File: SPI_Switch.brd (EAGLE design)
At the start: 71 x 62.2 mm, 40 parts, among them J1 8516-4500PL, J2 1-406525-1, J3 1-406525-1, J4 0705510037, J5 0705510037, U1 TLE7230G, U2 SN74ABT126

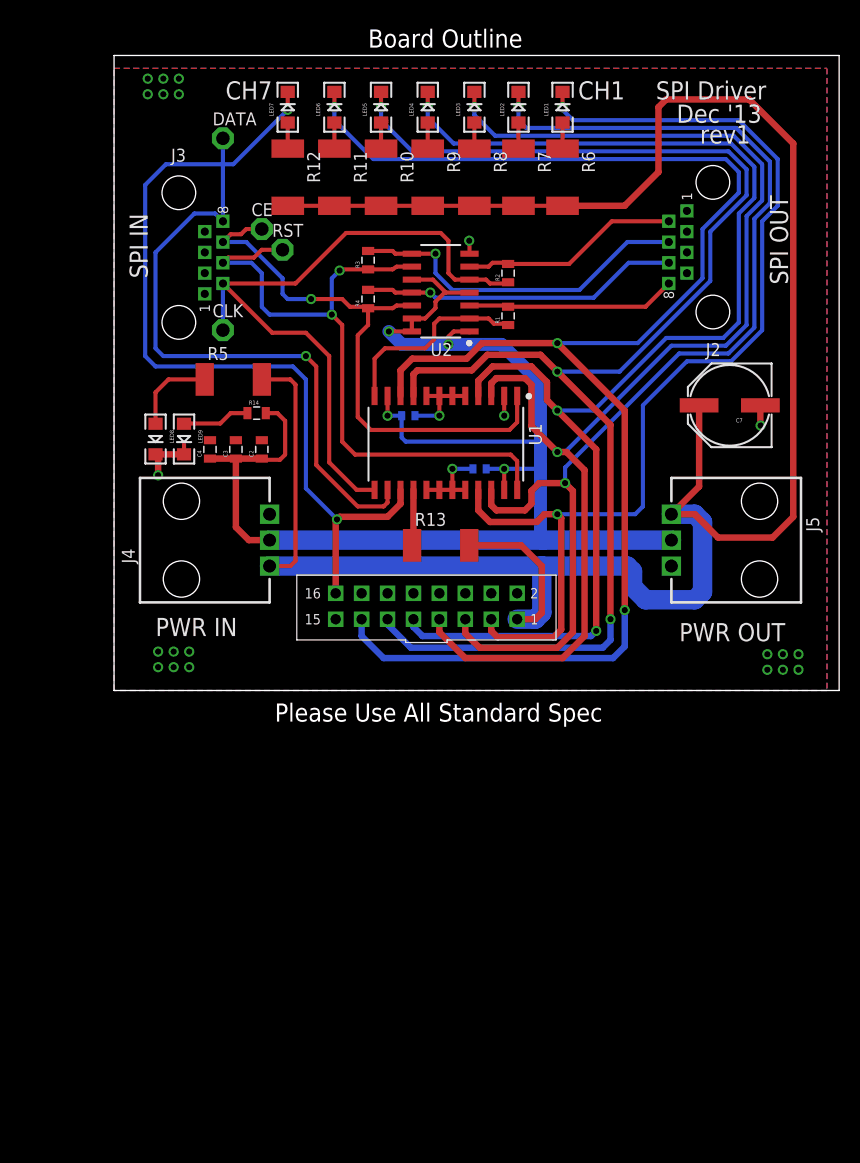
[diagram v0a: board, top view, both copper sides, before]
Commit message: Replaced decoupling caps for line driver with a larger package. Added smaller resistors for LEDs. Must ensure we never pull over 20mA with this resistor package.
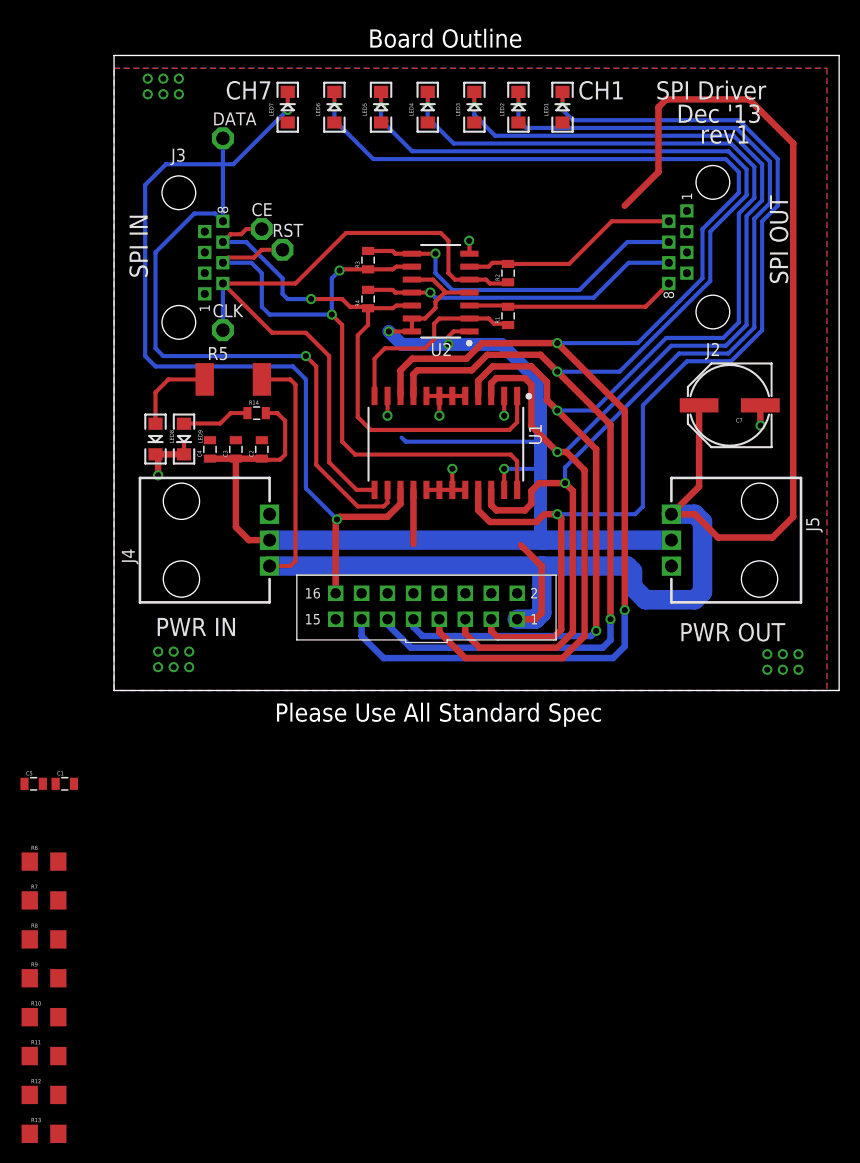
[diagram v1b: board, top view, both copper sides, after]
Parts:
- C1, C5: value (none) -> 10uF; device SparkFun-Passives:0402-CAP -> SparkFun-Passives:0805
- R10, R11, R12, R13, R6, R7, R8, R9: value 2k -> 1.5k; device SparkFun-Passives:R2512 -> SparkFun-Passives:1206
- moved R12 93.0 mm to (-6.86, -39.6), turned to 0 degrees
- moved R11 90.7 mm to (-6.86, -35.8), turned to 0 degrees
- moved R10 88.7 mm to (-6.86, -32.0), turned to 0 degrees
- moved R9 87.0 mm to (-6.86, -28.2), turned to 0 degrees
- moved R8 85.8 mm to (-6.86, -24.4), turned to 0 degrees
- moved R7 84.8 mm to (-6.86, -20.6), turned to 0 degrees
- moved R6 84.1 mm to (-6.86, -16.8), turned to 0 degrees
- moved R13 69.5 mm to (-6.86, -43.4)
- moved C5 53.5 mm to (-7.87, -9.14), flipped to the top
- moved C1 49.3 mm to (-4.83, -9.14), flipped to the top, turned to 0 degrees
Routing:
- net +24V: track 222.6 -> 184.5 mm
- net +5V: track 140.0 -> 134.7 mm
- net GND: track 27.3 -> 22.9 mm
- net N$7: track 4.03 -> 1.25 mm
- net N$9: track 2.56 -> 0.00 mm
- net N$8: track 2.56 -> 0.00 mm
- net N$6: track 2.56 -> 0.00 mm
- net N$5: track 2.56 -> 0.00 mm
- net N$3: track 2.56 -> 0.00 mm
- net N$1: track 2.56 -> 0.00 mm

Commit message: redoing layout
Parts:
- added H1, H2, H3, H4: MOUNT-HOLE2.8, holes:2,8
- moved J1 6.11 mm to (43.8, 2.67)
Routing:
- net CH6: track 153.5 -> 73.2 mm, vias 3 -> 2
- net CH5: track 141.4 -> 71.6 mm, vias 3 -> 2
- net CH4: track 128.8 -> 73.7 mm, vias 3 -> 2
- net CH3: track 123.2 -> 72.8 mm
- net +24V: track 184.5 -> 136.0 mm
- net CH2: track 110.6 -> 71.7 mm
- net CH1: track 106.1 -> 75.6 mm
- net CH7: track 82.7 -> 67.2 mm
- net CH8: track 5.30 -> 0.00 mm
- net GND: vias 23 -> 5

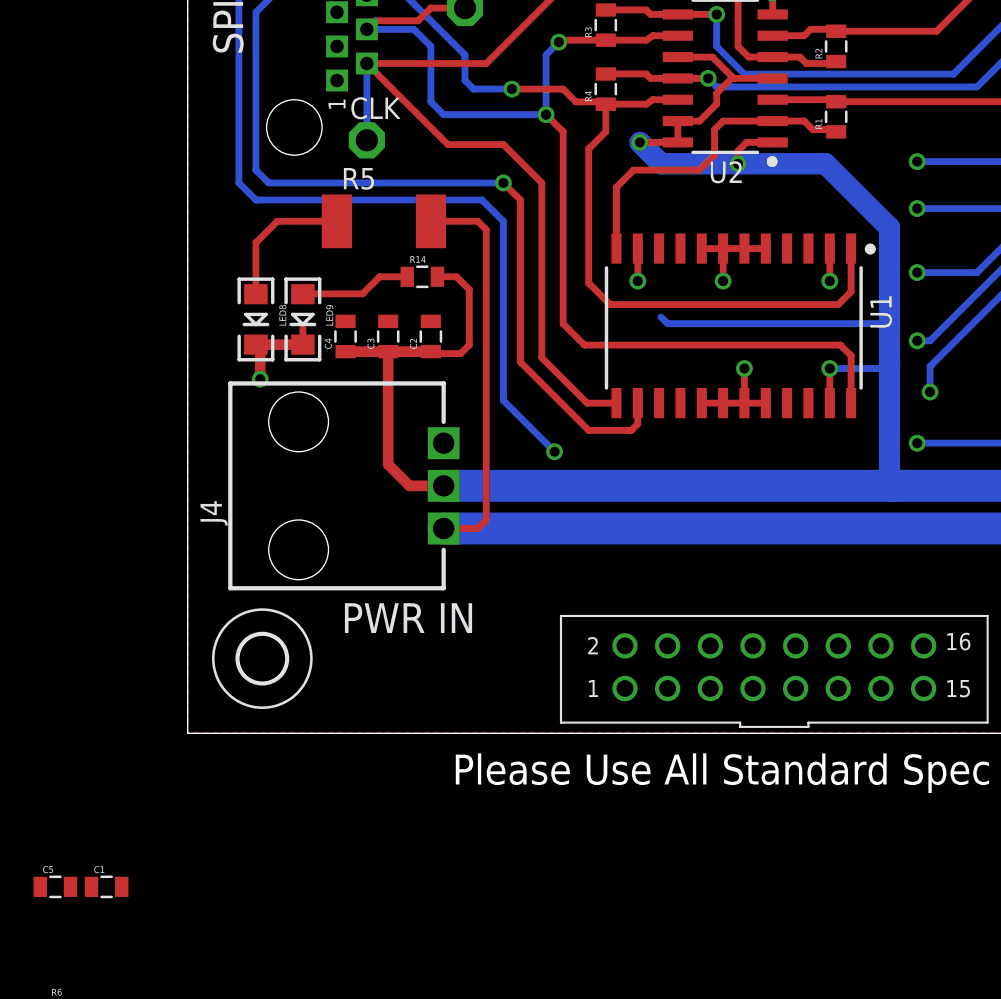
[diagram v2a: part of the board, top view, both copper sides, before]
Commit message: Redid layout again get rid of data out crossing 5V. Time to re-route.
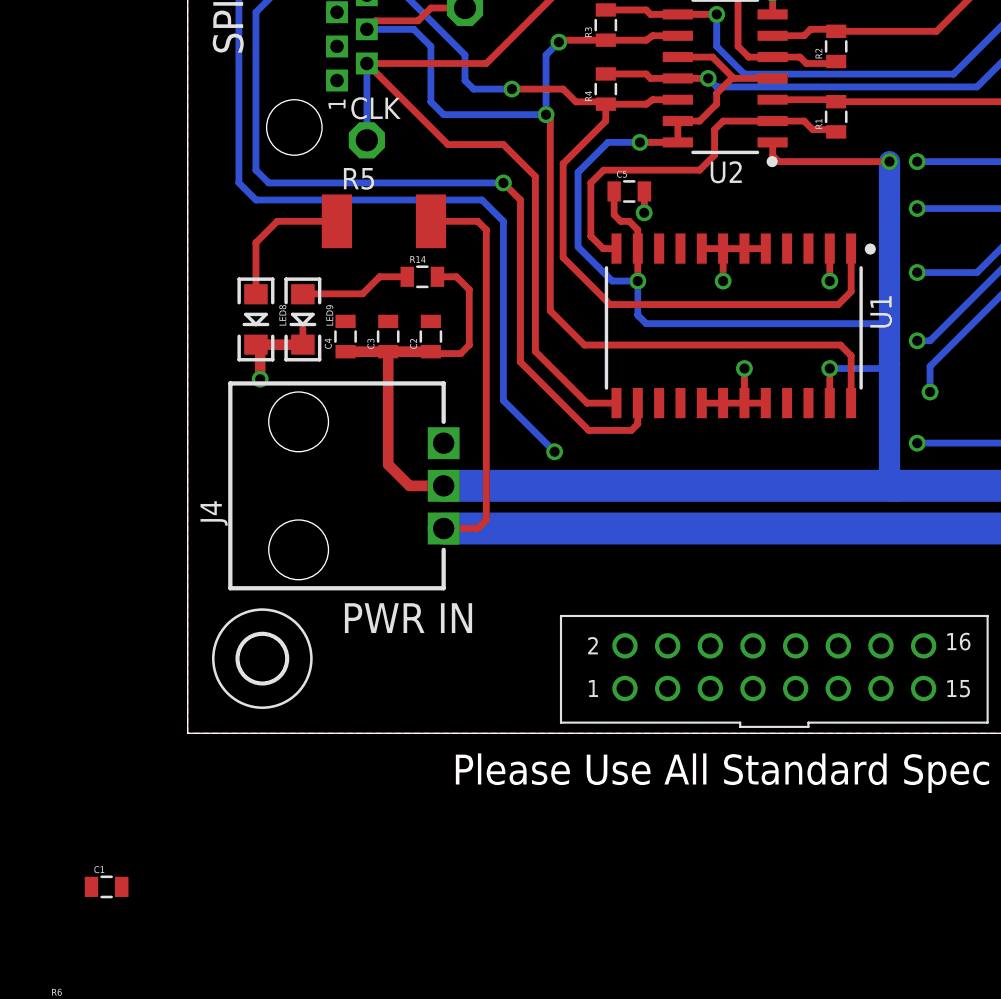
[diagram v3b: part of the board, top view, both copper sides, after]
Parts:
- moved C5 53.7 mm to (26.3, 32.3)
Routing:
- net +5V: track 134.7 -> 147.5 mm
- net DATA_OUT: track 19.5 -> 22.3 mm
- net GND: track 22.9 -> 24.2 mm, vias 5 -> 6
- net CE: track 56.7 -> 58.0 mm

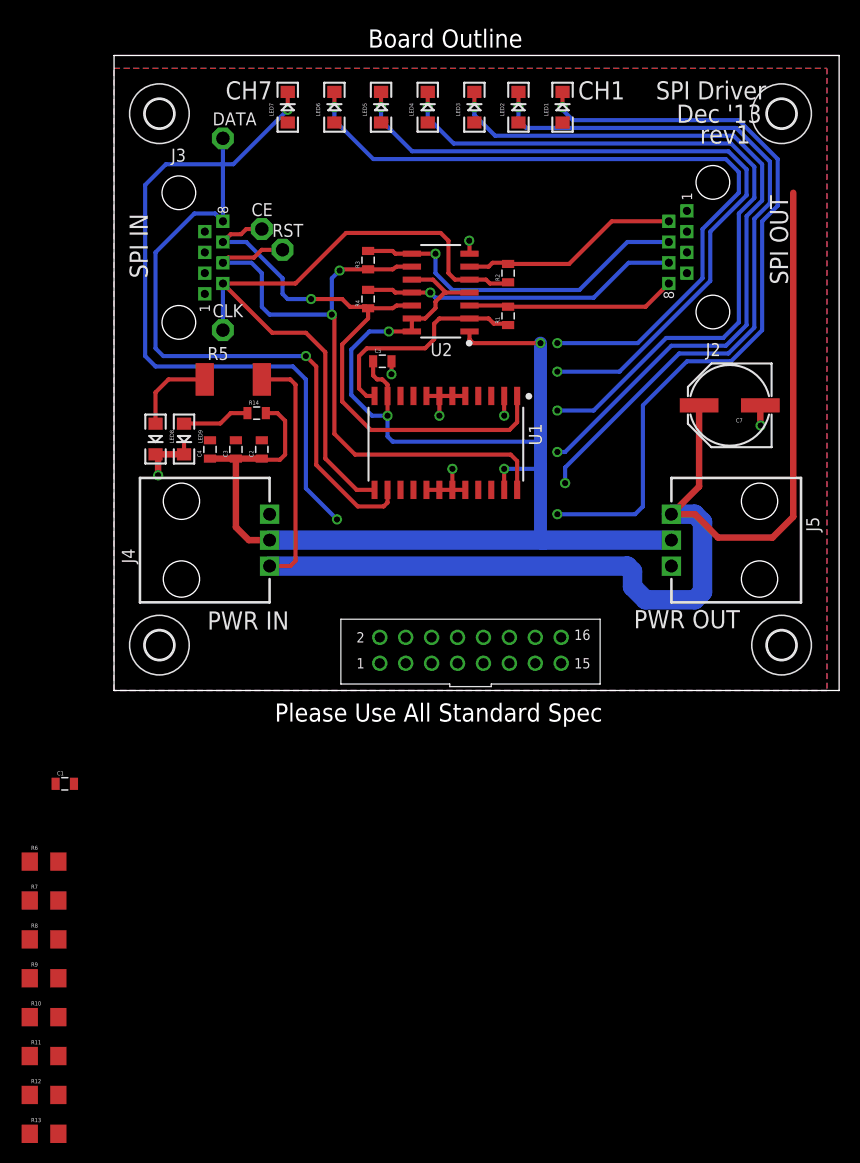
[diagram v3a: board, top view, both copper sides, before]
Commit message: re routed outputs and LEDs
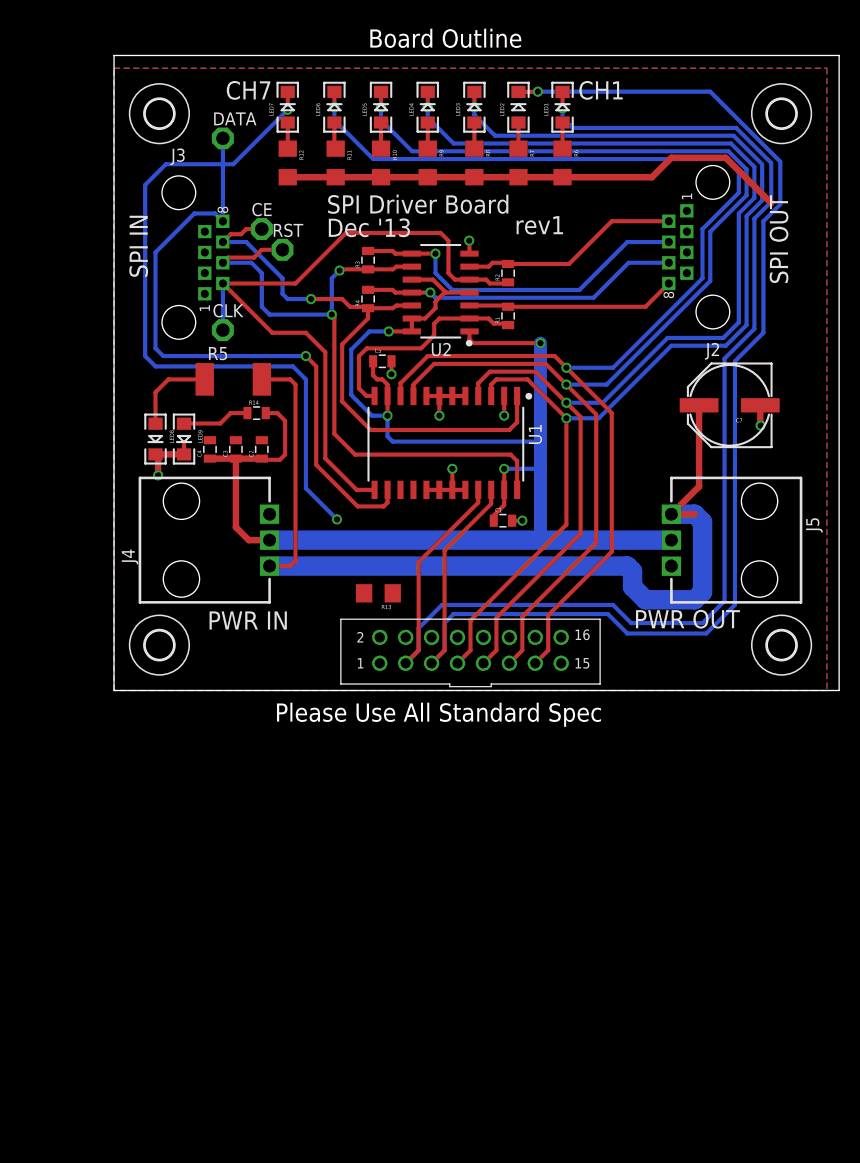
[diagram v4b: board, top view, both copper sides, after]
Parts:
- moved R12 94.4 mm to (17.0, 51.7), turned to 270 degrees
- moved R11 92.1 mm to (21.7, 51.7), turned to 270 degrees
- moved R10 90.0 mm to (26.2, 51.7), turned to 270 degrees
- moved R9 88.3 mm to (30.7, 51.7), turned to 270 degrees
- moved R8 87.0 mm to (35.3, 51.7), turned to 270 degrees
- moved R7 85.9 mm to (39.6, 51.7), turned to 270 degrees
- moved R6 85.2 mm to (43.9, 51.7), turned to 270 degrees
- moved R13 62.3 mm to (25.9, 9.53), turned to 180 degrees
- moved C1 50.1 mm to (38.1, 16.6)
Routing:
- net CH2: track 71.7 -> 128.4 mm, vias 2 -> 1
- net CH6: track 73.2 -> 126.3 mm
- net CH1: track 75.6 -> 126.1 mm, vias 2 -> 1
- net CH5: track 71.6 -> 121.1 mm
- net CH4: track 73.7 -> 114.2 mm
- net CH3: track 72.8 -> 109.0 mm
- net +24V: track 136.0 -> 142.8 mm
- net +5V: track 147.5 -> 151.0 mm
- net N$8: track 0.00 -> 2.61 mm
- net N$9: track 0.00 -> 2.56 mm
- net N$7: track 1.25 -> 3.81 mm
- net N$6: track 0.00 -> 2.56 mm
- net N$5: track 0.00 -> 2.56 mm
- net N$3: track 0.00 -> 2.56 mm
- net N$1: track 0.00 -> 2.56 mm
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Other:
- board text added: "SPI Driver Board"
- board text removed: "SPI Driver"

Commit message: finished take 2
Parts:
- moved H4 2.70 mm to (67.2, 58.5)
- moved H1 1.85 mm to (67.2, 3.94)
- moved H3 1.85 mm to (3.94, 58.3)
- moved H2 0.72 mm to (3.94, 3.94)
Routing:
- net CH7: track 67.2 -> 119.8 mm
- net +24V: track 142.8 -> 187.1 mm
- net CH8: track 0.00 -> 11.0 mm
- net GND: track 25.2 -> 22.2 mm, vias 7 -> 28
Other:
- board text added: "Dec 2013"
- board text removed: "Dec '13"

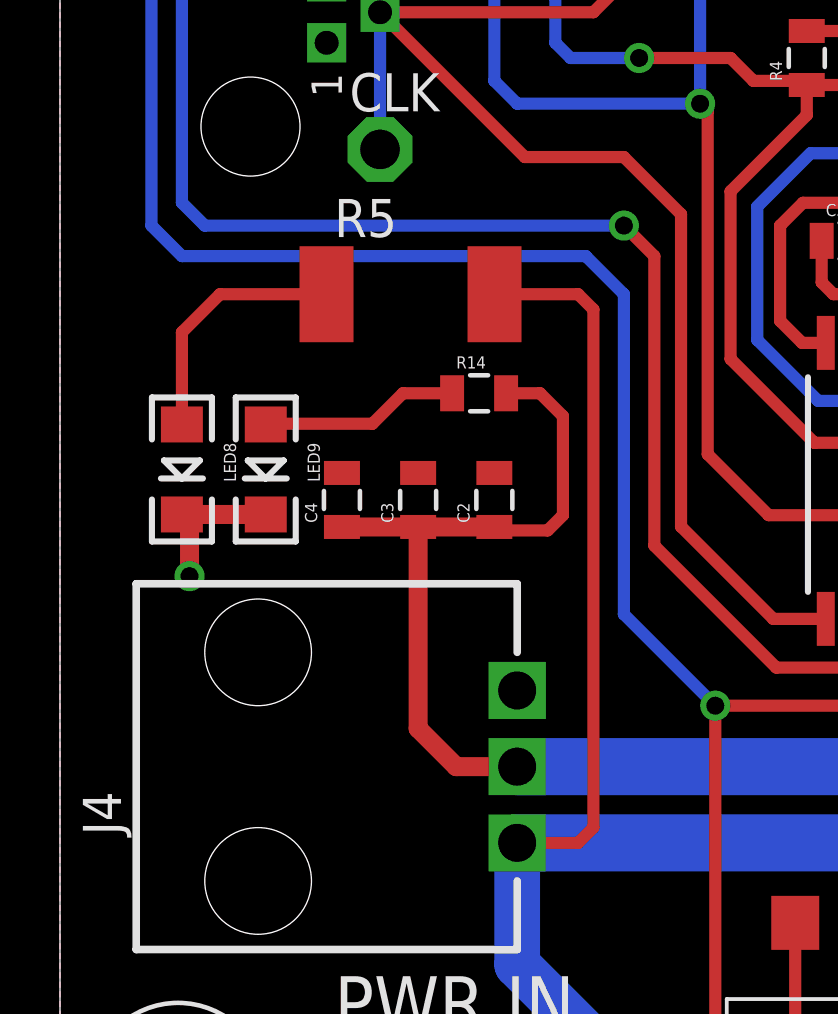
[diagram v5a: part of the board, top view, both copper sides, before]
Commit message: Switched the footprint for R5 to be smaller
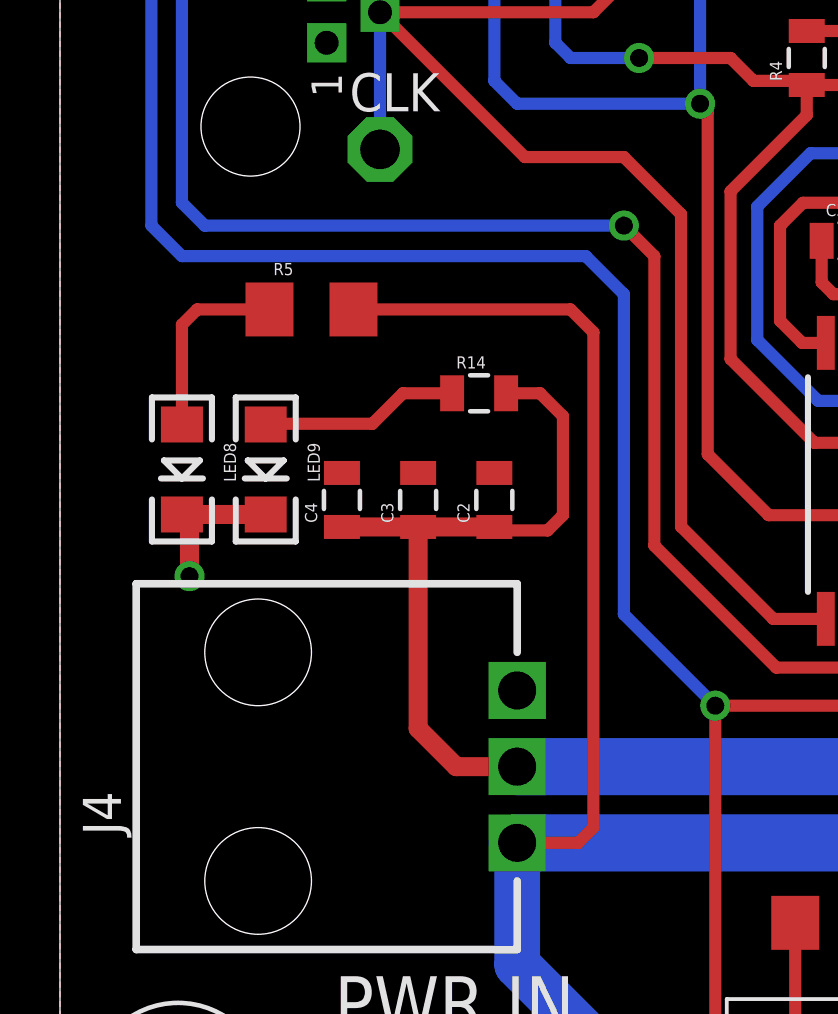
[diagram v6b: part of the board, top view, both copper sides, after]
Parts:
- R5: value 2k -> 1.5k; device SparkFun-Passives:R2512 -> SparkFun-Passives:1206
- moved R5 3.34 mm to (8.38, 30.0)
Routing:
- net +24V: track 187.1 -> 191.1 mm
- net N$2: track 8.42 -> 6.45 mm
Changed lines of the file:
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@@
 <element name="LED8" library="SparkFun-LED" package="LED-1206" value="YELLOW" x="4.064" y="24.638" rot="R270"/>
 <element name="LED9" library="SparkFun-LED" package="LED-1206" value="YELLOW" x="6.858" y="24.638" rot="R270"/>
-<element name="R5" library="SparkFun-Passives" package="R2512" value="2k" x="11.684" y="30.48"/>
 <element name="R14" library="SparkFun-Passives" package="0805" value="330" x="13.97" y="27.178"/>
 <element name="C1" library="SparkFun-Passives" package="0805" value="10uF" x="38.1" y="16.637"/>
@@
 <element name="H3" library="holes" package="2,8" value="MOUNT-HOLE2.8" x="3.937" y="58.293"/>
 <element name="H4" library="holes" package="2,8" value="MOUNT-HOLE2.8" x="67.183" y="58.547"/>
+<element name="R5" library="SparkFun-Passives" package="1206" value="1.5k" x="8.382" y="29.972"/>
 </elements>
 <signals>
@@
 <contactref element="J4" pad="P$1"/>
 <contactref element="C7" pad="+"/>
-<contactref element="R5" pad="2"/>
 <wire x1="15.24" y1="12.192" x2="50.292" y2="12.192" width="1.905" layer="16"/>
 <wire x1="50.8" y1="10.16" x2="52.07" y2="8.89" width="1.905" layer="16"/>
@@
 <wire x1="50.8" y1="10.16" x2="50.8" y2="11.684" width="1.905" layer="16"/>
 <wire x1="50.8" y1="11.684" x2="50.292" y2="12.192" width="1.905" layer="16"/>
-<wire x1="14.484" y1="30.48" x2="17.272" y2="30.48" width="0.4064" layer="1"/>
-<wire x1="17.272" y1="30.48" x2="17.78" y2="29.972" width="0.4064" layer="1"/>
-<wire x1="17.78" y1="29.972" x2="17.78" y2="12.7" width="0.4064" layer="1"/>
+<wire x1="17.78" y1="29.21" x2="17.78" y2="12.7" width="0.4064" layer="1"/>
 <wire x1="17.78" y1="12.7" x2="17.272" y2="12.192" width="0.4064" layer="1"/>
 <wire x1="17.272" y1="12.192" x2="15.24" y2="12.192" width="0.4064" layer="1"/>
@@
 <wire x1="15.24" y1="8.128" x2="20.701" y2="2.667" width="1.524" layer="16"/>
 <wire x1="20.701" y1="2.667" x2="26.035" y2="2.667" width="1.524" layer="16"/>
+<contactref element="R5" pad="2"/>
+<wire x1="9.782" y1="29.972" x2="17.018" y2="29.972" width="0.4064" layer="1"/>
+<wire x1="17.018" y1="29.972" x2="17.78" y2="29.21" width="0.4064" layer="1"/>
 </signal>
 <signal name="+5V">
@@
 <signal name="N$2">
 <contactref element="LED8" pad="A"/>
+<wire x1="4.064" y1="29.464" x2="4.064" y2="26.138" width="0.4064" layer="1"/>
 <contactref element="R5" pad="1"/>
-<wire x1="8.884" y1="30.48" x2="5.334" y2="30.48" width="0.4064" layer="1"/>
-<wire x1="5.334" y1="30.48" x2="4.064" y2="29.21" width="0.4064" layer="1"/>
-<wire x1="4.064" y1="29.21" x2="4.064" y2="26.138" width="0.4064" layer="1"/>
+<wire x1="4.064" y1="29.464" x2="4.572" y2="29.972" width="0.4064" layer="1"/>
+<wire x1="4.572" y1="29.972" x2="6.982" y2="29.972" width="0.4064" layer="1"/>
 </signal>
 <signal name="N$4">
